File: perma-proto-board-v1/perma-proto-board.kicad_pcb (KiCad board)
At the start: 2 copper layers, 156.2 x 81.3 mm, 50 parts, among them J1 SPI_01, J10 I2C_04, J11 I2C_05, J12 I2C_06, J13 A_1, J14 A_2, J15 A_3, J16 A_4, J17 A_5, J18 B_1, J19 B_2, J2 SPI_02, J20 B_3, J21 B_4, J22 B_5, J23 C_1, J24 C_2, J25 C_3, J26 C_4, J27 C_5, J28 Power01, J29 Power02, J3 SPI_03, J30 Power03, J31 Power04, J32 Rail01, J33 Rail02, J36 Rail05, J37 Rail06, J4 SPI_04, J40 USB_C_Receptacle, J41 SPI_CS_01, J42 SPI_CS_02, J43 SPI_CS_03, J44 SPI_CS_04, J45 SPI_CS_05, J46 SPI_CS_06, J5 SPI_05, J6 SPI_06, J7 I2C_01, J8 I2C_02, J9 I2C_03

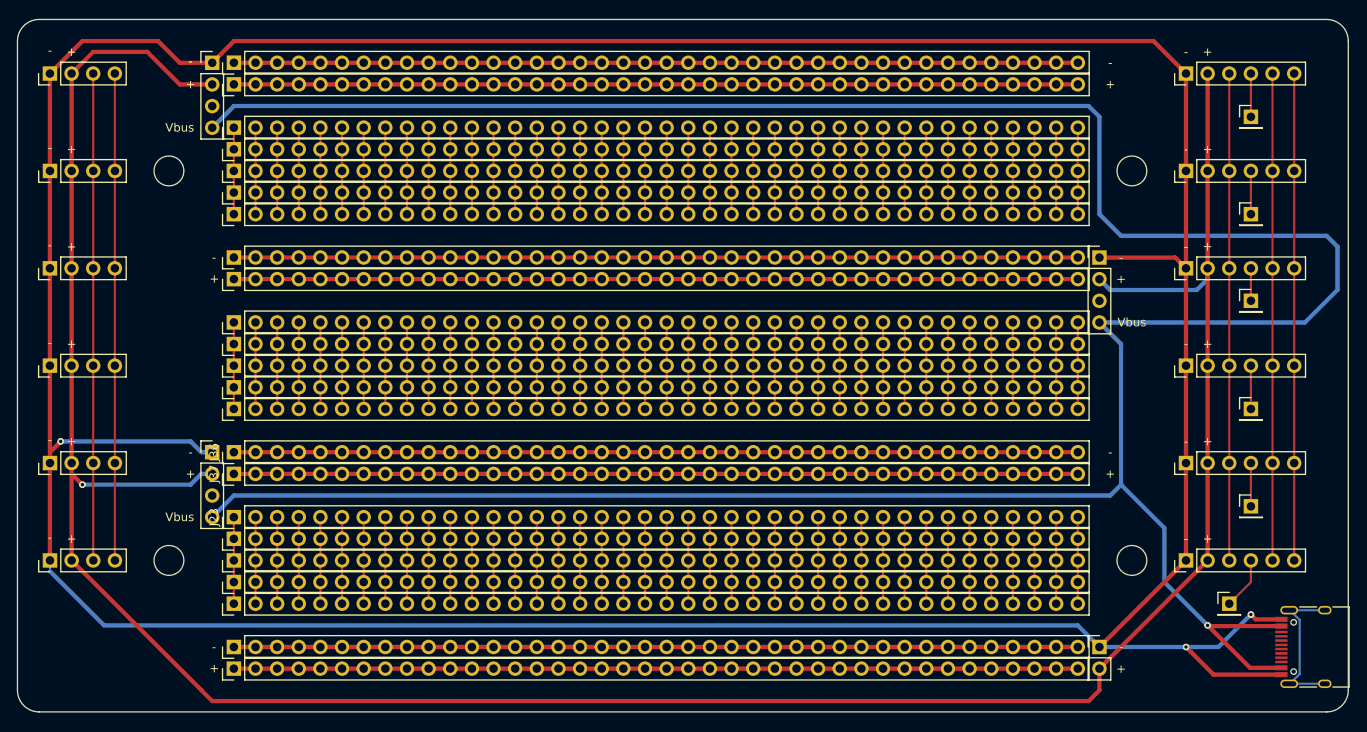
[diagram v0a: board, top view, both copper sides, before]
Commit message: added github url to silk screen
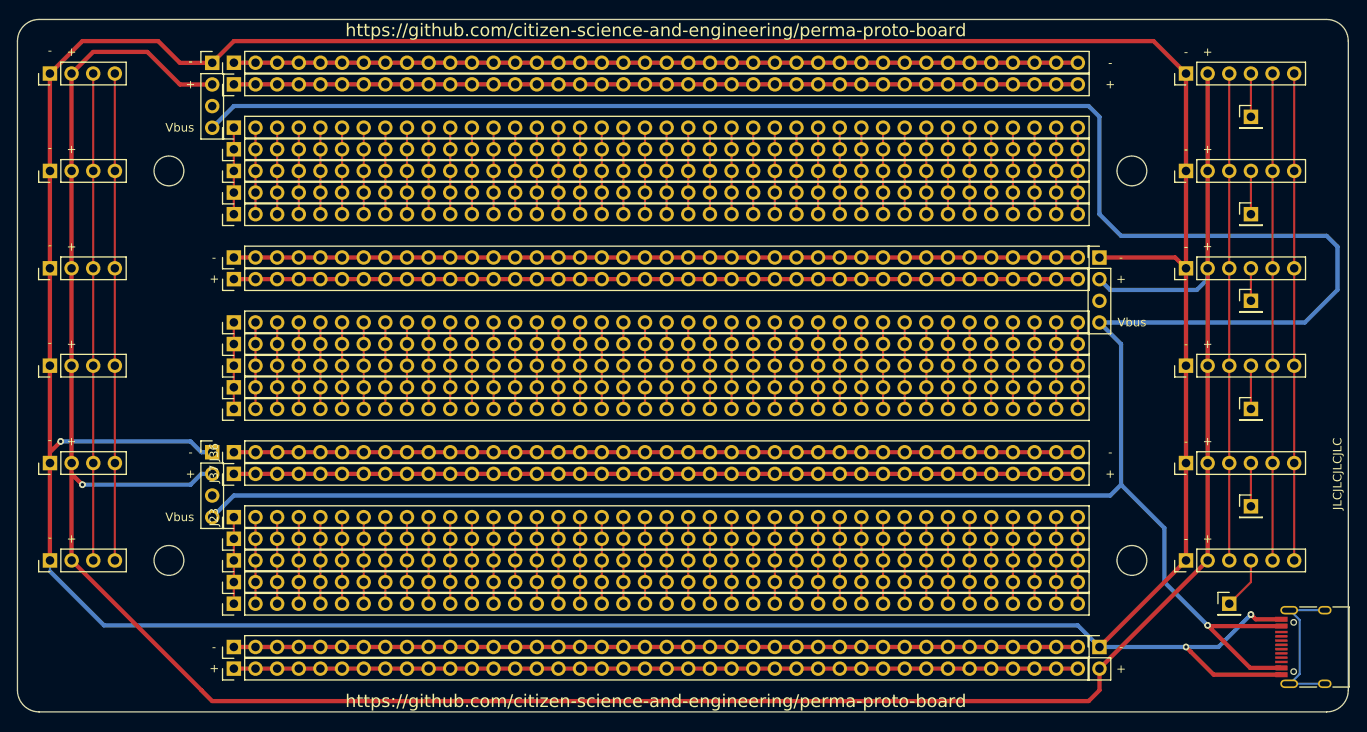
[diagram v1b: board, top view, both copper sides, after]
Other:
- board text added: "JLCJLCJLCJLC"
- board text added: "https://github.com/citizen-science-and-engineering/perma-proto-board"
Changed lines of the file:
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@@
+    (effects (font (size 1 1) (thickness 0.15)))
+  )
+  (gr_text "JLCJLCJLCJLC" (at 200.66 81.28 90) (layer "F.SilkS")
     (effects (font (size 1 1) (thickness 0.15)))
   )
@@
   (gr_text "-" (at 182.88 54.61) (layer "F.SilkS")
     (effects (font (size 1 1) (thickness 0.15)))
+  )
+  (gr_text "https://github.com/citizen-science-and-engineering/perma-proto-board" (at 120.65 29.21) (layer "F.SilkS")
+    (effects (font (size 1.5 1.5) (thickness 0.3)))
   )
   (gr_text "+" (at 185.42 43.18) (layer "F.SilkS")
@@
     (effects (font (size 1 1) (thickness 0.15)))
   )
+  (gr_text "https://github.com/citizen-science-and-engineering/perma-proto-board" (at 120.65 107.95) (layer "F.SilkS")
+    (effects (font (size 1.5 1.5) (thickness 0.3)))
+  )
   (segment (start 179.07 30.48) (end 71.13 30.48) (width 0.5) (layer "F.Cu") (net 1))
